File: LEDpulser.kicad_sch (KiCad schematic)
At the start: 61 parts, among them J1 RJ45_Shielded, J2 EPS.00.250.NTN, J3 EPS.00.250.NTN, J4 Conn_01x04_Female, J5 LED, Q1 AO3401A, Q2 AO3400A, Q3 AO3400A, SW1 ATE1D-5M3-10-Z, U1 74HC123, U10 LT3082, U2 74HC123, U3 74HC123, U4 74HC10, U5 LT1121-5, U6 PM8834, U7 NE555, U8 PM8834, U9 PM8834

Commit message: Fixed open connection, grounded unused inputs, adjusted connector facing.
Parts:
- removed R5: 100k, Resistor_SMD:R_0603_1608Metric, symbol Device:R
- added unit 2 of U1
- added unit 2 of U4
- added unit 3 of U4
- J1: value RJ45_Shielded -> RJHSE5380; footprint Connector_RJ:RJ45_Amphenol_RJHSE538X -> Connector_RJ:RJ45_Amphenol_RJHSE5380
- R8: value 50 -> 100k
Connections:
- net GND: now also U6.4 (IN_B), U1.10 (B), U1.11 (Clr), U1.9 (A), U4.11, U4.12, U4.13, U4.3, U4.4, U4.5
- net LED_ON: now also Q2.1 (G)

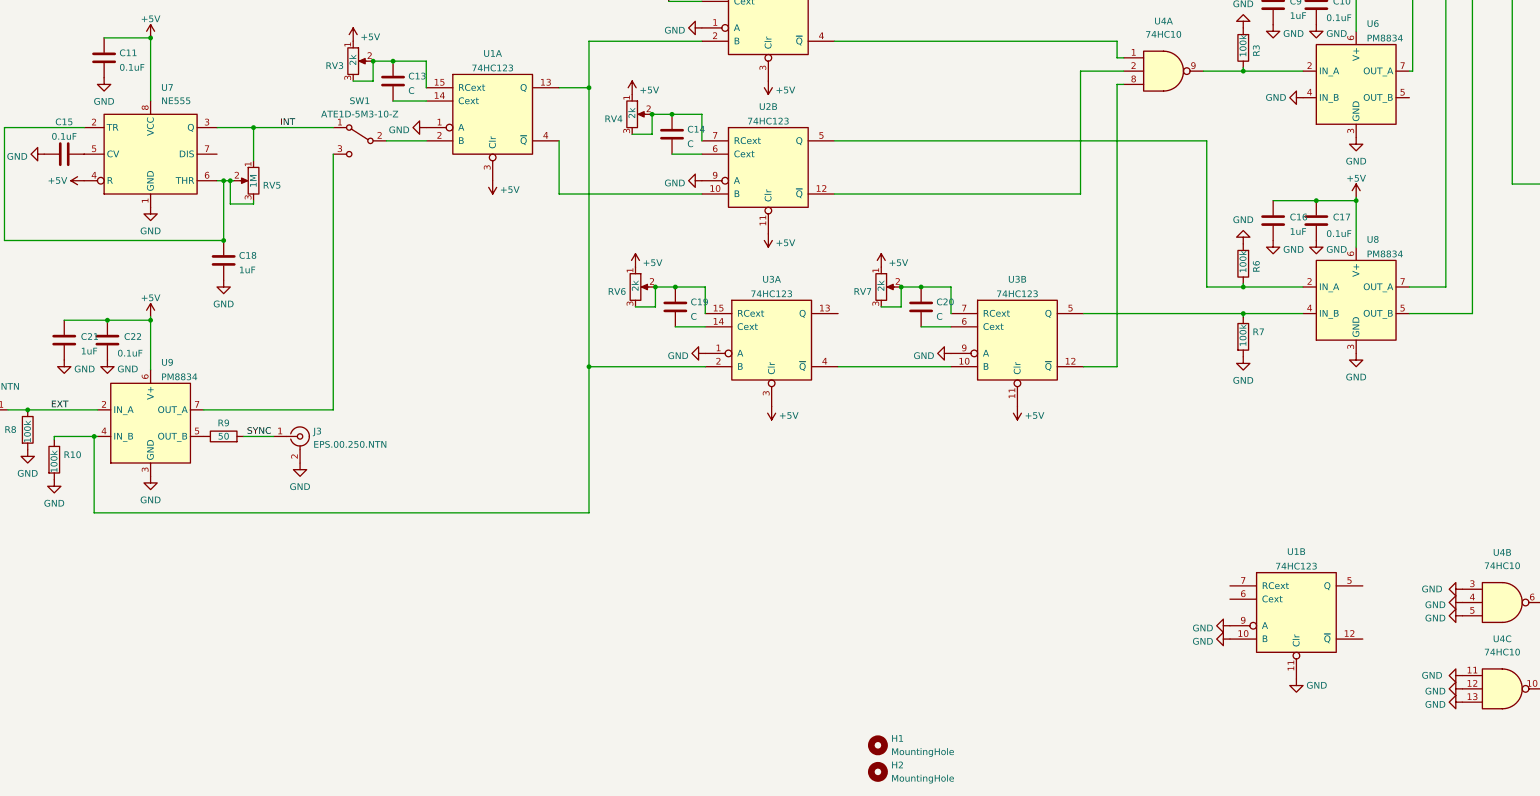
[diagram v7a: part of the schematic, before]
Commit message: Changed switch, added sync pulse monostable, rerouted.
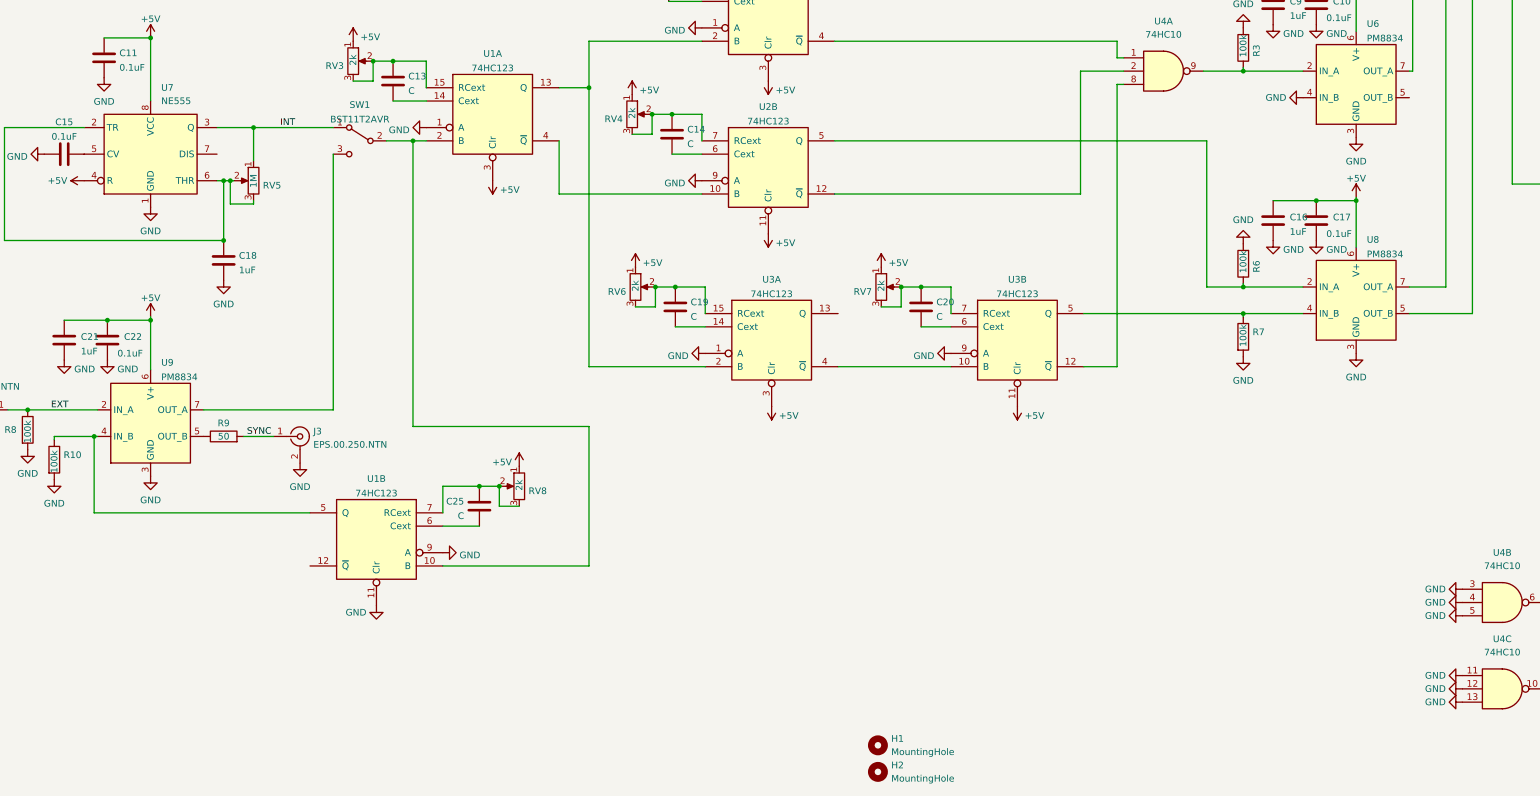
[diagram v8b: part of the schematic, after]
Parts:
- added C25: C, Capacitor_SMD:C_0603_1608Metric, symbol Device:C
- added RV8: 2k, Potentiometer_THT:Potentiometer_Bourns_3266X_Horizontal, symbol Device:R_Potentiometer
- SW1: value ATE1D-5M3-10-Z -> BST11T2AVR; PartNumber (none) -> BST11T2AVR
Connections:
- net +5V: now also RV8.1
- net GND: no longer U1.10 (B)
- net at U1.13 (Q), U2.2 (B), U3.2 (B): no longer R10.1, U9.4 (IN_B)
- net at U1.5 (Q): now also R10.1, U9.4 (IN_B)
- net at U1.6 (Cext): now also C25.2
- net at U1.7 (RCext): now also C25.1, RV8.2, RV8.3
- net at SW1.2 (B), U1.2 (B): now also U1.10 (B)
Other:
- moved on the sheet: U1B
